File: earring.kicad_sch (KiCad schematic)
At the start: 98 parts, among them J2 USB_C_Receptacle_USB2.0, Q1 NMOS 20V 0.75A 500mΩ@4.5V, Q2 NMOS 20V 0.75A 500mΩ@4.5V, Q3 NMOS 20V 0.75A 500mΩ@4.5V, Q4 NMOS 20V 0.75A 500mΩ@4.5V, U1 Magnetic Switch, U10 USBLC6-2P6, U20 LGS4056H, U3 RP2040, U4 W25Q16JV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

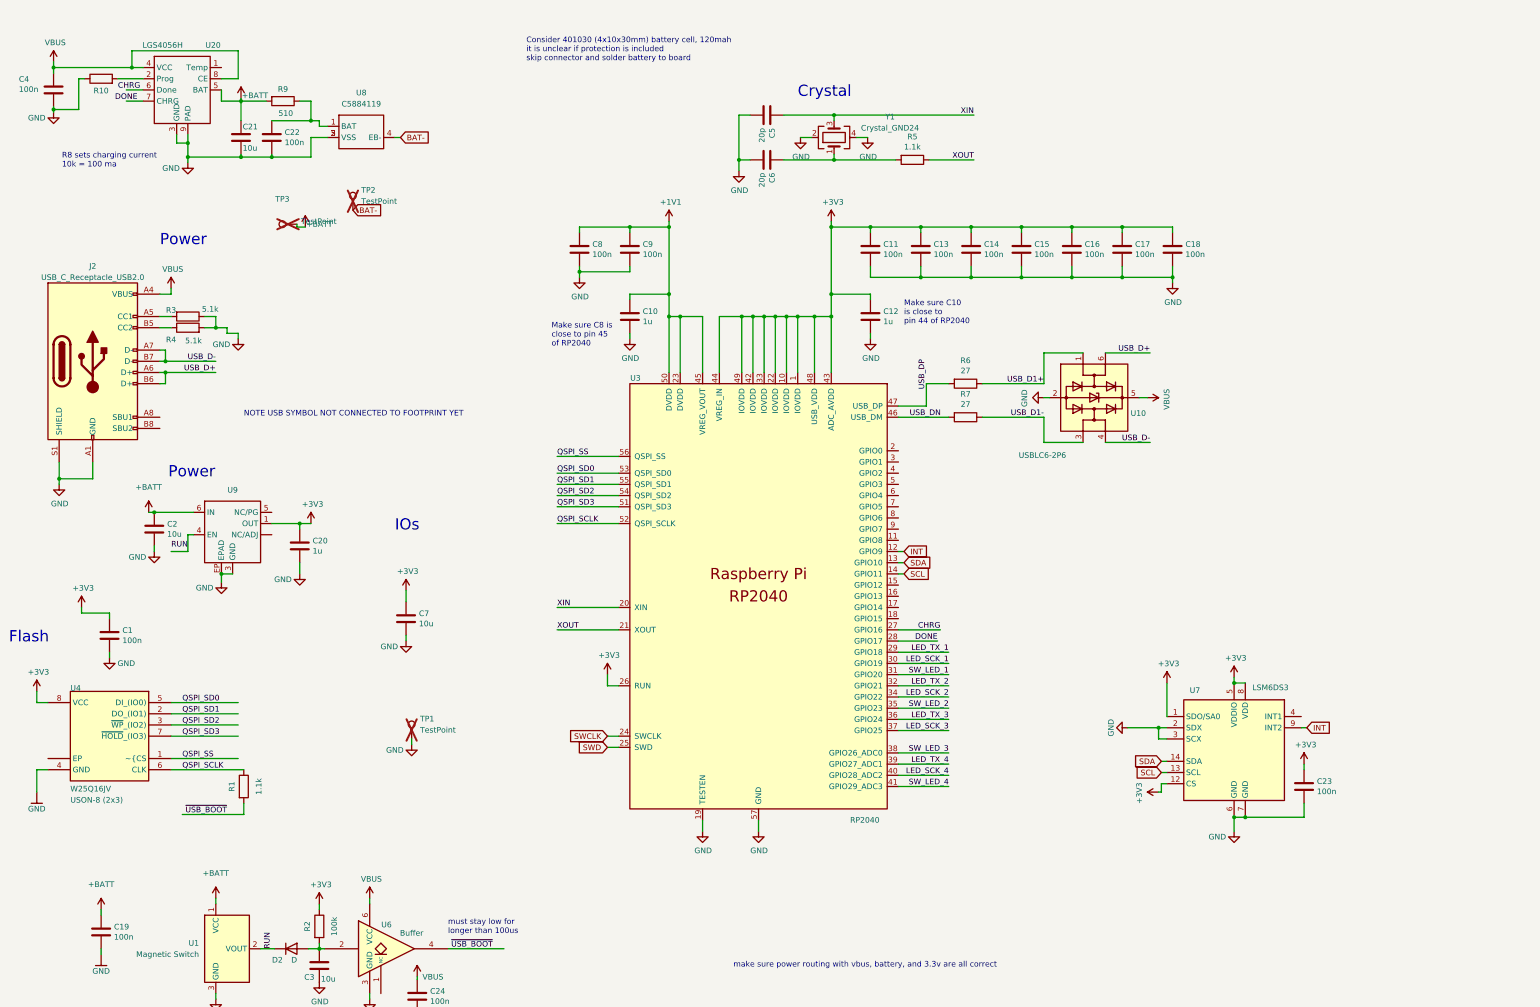
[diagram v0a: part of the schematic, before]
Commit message: Updated files, nearly complete. Added stiffener layer.
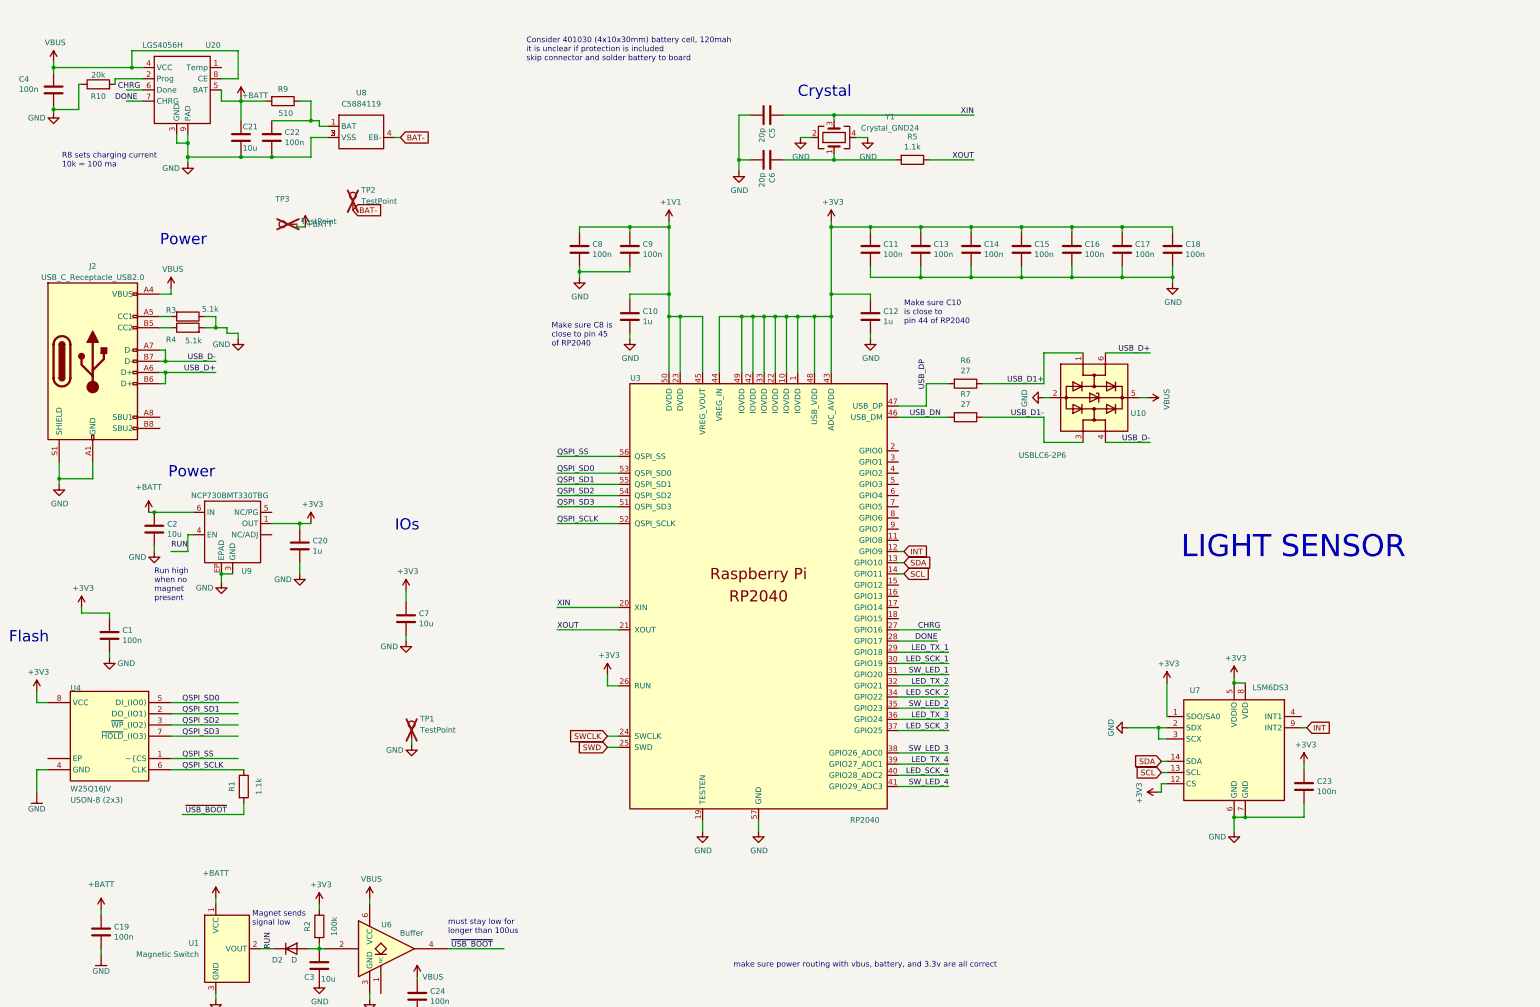
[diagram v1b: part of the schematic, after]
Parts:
- C1, C11, C13, C14, C15, C16, C17, C18, C19, C22, C23, C24, C4, C8, C9: LCSC C30926 -> C60474
- C10, C12, C20, C25, C26, C27, C28, C29, C30, C31, C32: LCSC C15849 -> C29266
- C2: LCSC C15850 -> C315248
- C5, C6: LCSC C1648 -> C107000
- R10: value ~ -> 20k; LCSC (none) -> C25765
- U6: LCSC C7598681 -> C2864615
- U9: value ~ -> NCP730BMT330TBG; LCSC (none) -> C892821
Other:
- note added: "LIGHT SENSOR"
- note added: "Magnet sends signal low"
- note added: "Run high when no magnet present"
- note removed: "NOTE USB SYMBOL NOT CONNECTED TO FOOTPRINT YET"
- moved on the sheet: R10

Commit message: Add light sensor, add more 3d models.
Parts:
- added Q5: ~, LED_SMD:LED_0603_1608Metric, symbol Sensor_Optical:KPS-3227
- added R8: WHAT VALUE?, Resistor_SMD:R_0402_1005Metric, symbol Device:R
- R3, R4: LCSC C137955 -> C25905
- U24: value ~ -> SK9822-EC20
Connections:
- net +3V3: now also Q5.1, Q5.3
- net GND: now also R8.2
- net SW_LED_3: now also U3.2 (GPIO0); no longer U3.38 (GPIO26_ADC0)
- new net LIGHT_SENSE: Q5.2, Q5.4, R8.1, U3.38 (GPIO26_ADC0)
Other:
- note removed: "LIGHT SENSOR"
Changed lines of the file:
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@@
   (junction (at 543.56 27.94) (diameter 0) (color 0 0 0 0)
   )
+  (junction (at 316.865 144.78) (diameter 0) (color 0 0 0 0)
+  )
   (junction (at 280.67 188.595) (diameter 0) (color 0 0 0 0)
   )
@@
     (stroke (width 0) (type default))
   )
+  (wire (pts (xy 316.865 156.21) (xy 316.865 153.035))
+    (stroke (width 0) (type default))
+  )
   (wire (pts (xy 202.565 107.95) (xy 202.565 95.25))
     (stroke (width 0) (type default))
@@
     (stroke (width 0) (type default))
   )
+  (wire (pts (xy 313.69 144.78) (xy 316.865 144.78))
+    (stroke (width 0) (type default))
+  )
   (wire (pts (xy 281.305 203.2) (xy 280.67 203.2))
     (stroke (width 0) (type default))
@@
     (stroke (width 0) (type default))
   )
+  (wire (pts (xy 316.865 132.08) (xy 316.865 133.985))
+    (stroke (width 0) (type default))
+  )
   (wire (pts (xy 464.82 83.82) (xy 482.6 83.82))
     (stroke (width 0) (type default))
@@
     (stroke (width 0) (type default))
   )
+  (wire (pts (xy 316.865 144.78) (xy 316.865 144.145))
+    (stroke (width 0) (type default))
+  )
   (wire (pts (xy 378.46 185.42) (xy 383.54 185.42))
     (stroke (width 0) (type default))
@@
     (stroke (width 0) (type default))
   )
+  (wire (pts (xy 316.865 145.415) (xy 316.865 144.78))
+    (stroke (width 0) (type default))
+  )
   (wire (pts (xy 574.04 195.58) (xy 579.12 195.58))
     (stroke (width 0) (type default))
@@
     (stroke (width 0) (type default))
   )
-  (wire (pts (xy 221.615 194.31) (xy 233.045 194.31))
+  (wire (pts (xy 221.615 125.73) (xy 233.045 125.73))
     (stroke (width 0) (type default))
   )
@@
     (stroke (width 0) (type default))
   )
+  (wire (pts (xy 221.615 194.31) (xy 234.95 194.31))
+    (stroke (width 0) (type default))
+  )
   (wire (pts (xy 36.195 161.29) (xy 36.195 162.56))
     (stroke (width 0) (type default))
@@
     (effects (font (size 1.27 1.27)) (justify left bottom))
   )
-  (text "LIGHT SENSOR" (at 285.75 150.495 0)
-    (effects (font (size 5 5)) (justify left bottom))
-  )
   (text "need to double check RC\nrise time considering\nbuffer flips at less than 0.7v"
     (at 72.39 259.715 0)
@@
     (effects (font (size 1.27 1.27)) (justify left bottom))
   )
-  (label "SW_LED_3" (at 233.045 194.31 180) (fields_autoplaced)
+  (label "SW_LED_3" (at 233.045 125.73 180) (fields_autoplaced)
     (effects (font (size 1.27 1.27)) (justify right bottom))
   )
@@
     (effects (font (size 1.27 1.27)) (justify right bottom))
   )
+  (label "LIGHT_SENSE" (at 313.69 144.78 180) (fields_autoplaced)
+    (effects (font (size 1.27 1.27)) (justify right bottom))
+  )
   (label "LED_SCK_1" (at 520.7 226.06 180) (fields_autoplaced)
     (effects (font (size 1.27 1.27)) (justify right bottom))
@@
     (effects (font (size 1.27 1.27)) (justify right bottom))
   )
+  (label "LIGHT_SENSE" (at 234.95 194.31 180) (fields_autoplaced)
+    (effects (font (size 1.27 1.27)) (justify right bottom))
+  )
   (label "DONE" (at 230.505 168.91 180) (fields_autoplaced)
     (effects (font (size 1.27 1.27)) (justify right bottom))
@@
     )
   )
+  (symbol (lib_id "power:+3V3") (at 316.865 132.08 0) (unit 1)
+    (in_bom yes) (on_board yes) (dnp no)
+    (property "Reference" "#PWR050" (at 316.865 135.89 0)
+      (effects (font (size 1.27 1.27)) hide)
+    )
+    (property "Value" "+3V3" (at 317.246 127.6858 0)
+      (effects (font (size 1.27 1.27)))
+    )
+    (property "Footprint" "" (at 316.865 132.08 0)
+      (effects (font (size 1.27 1.27)) hide)
+    )
+    (property "Datasheet" "" (at 316.865 132.08 0)
+      (effects (font (size 1.27 1.27)) hide)
+    )
+    (pin "1")
+    (instances
+      (project "earring"
+        (path "/10ff4ace-8dac-45ce-94a5-ae8ae7d42914"
+          (reference "#PWR050") (unit 1)
+        )
+      )
+    )
+  )
   (symbol (lib_id "earring:SK9822") (at 561.34 73.66 0) (unit 1)
     (in_bom yes) (on_board yes) (dnp no) (fields_autoplaced)
@@
     )
   )
+  (symbol (lib_id "Device:R") (at 316.865 149.225 0) (unit 1)
+    (in_bom yes) (on_board yes) (dnp no)
+    (property "Reference" "R8" (at 313.5122 150.495 90)
+      (effects (font (size 1.27 1.27)))
+    )
+    (property "Value" "WHAT VALUE?" (at 324.0786 146.05 0)
+      (effects (font (size 1.27 1.27)))
+    )
+    (property "Footprint" "Resistor_SMD:R_0402_1005Metric" (at 315.087 149.225 90)
+      (effects (font (size 1.27 1.27)) hide)
+    )
+    (property "Datasheet" "~" (at 316.865 149.225 0)
+      (effects (font (size 1.27 1.27)) hide)
+    )
+    (property "LCSC" "" (at 316.865 149.225 90)
+      (effects (font (size 1.27 1.27)) hide)
+    )
+    (pin "1")
+    (pin "2")
+    (instances
+      (project "earring"
+        (path "/10ff4ace-8dac-45ce-94a5-ae8ae7d42914"
+          (reference "R8") (unit 1)
+        )
+      )
+    )
+  )
   (symbol (lib_id "earring:SK9822") (at 480.06 162.56 0) (unit 1)
     (in_bom yes) (on_board yes) (dnp no) (fields_autoplaced)
@@
       (effects (font (size 1.27 1.27)) (justify left))
     )
-    (property "Value" "~" (at 440.69 35.56 0)
-      (effects (font (size 1.27 1.27)))
+    (property "Value" "SK9822-EC20" (at 440.69 35.56 0)
+      (effects (font (size 1.27 1.27)) hide)
     )
     (property "Footprint" "parts:LED-SK9822-EC20" (at 440.69 35.56 0)
@@
       (effects (font (size 1.27 1.27)) hide)
     )
-    (property "LCSC" "C137955" (at 60.325 97.79 90)
+    (property "LCSC" "C25905" (at 60.325 97.79 90)
       (effects (font (size 1.27 1.27)) hide)
     )
@@
       (effects (font (size 1.27 1.27)) hide)
     )
-    (property "LCSC" "C137955" (at 60.325 95.25 90)
+    (property "LCSC" "C25905" (at 60.325 95.25 90)
       (effects (font (size 1.27 1.27)) hide)
     )
@@
     )
   )
+  (symbol (lib_id "power:GND") (at 316.865 156.21 0) (unit 1)
+    (in_bom yes) (on_board yes) (dnp no)
+    (property "Reference" "#PWR053" (at 316.865 162.56 0)
+      (effects (font (size 1.27 1.27)) hide)
+    )
+    (property "Value" "GND" (at 313.055 157.48 0)
+      (effects (font (size 1.27 1.27)))
+    )
+    (property "Footprint" "" (at 316.865 156.21 0)
+      (effects (font (size 1.27 1.27)) hide)
+    )
+    (property "Datasheet" "" (at 316.865 156.21 0)
+      (effects (font (size 1.27 1.27)) hide)
+    )
+    (pin "1")
+    (instances
+      (project "earring"
+        (path "/10ff4ace-8dac-45ce-94a5-ae8ae7d42914"
+          (reference "#PWR053") (unit 1)
+        )
+      )
+    )
+  )
   (symbol (lib_id "power:+BATT") (at 525.78 93.98 0) (unit 1)
     (in_bom yes) (on_board yes) (dnp no)
@@
         )
       )
+    )
+  )
+  (symbol (lib_id "Sensor_Optical:KPS-3227") (at 316.865 139.065 0) (unit 1)
+    (in_bom yes) (on_board yes) (dnp no) (fields_autoplaced)
+    (property "Reference" "Q5" (at 320.04 137.0457 0)
+      (effects (font (size 1.27 1.27)) (justify left))
+    )
+    (property "Value" "~" (at 320.04 139.5857 0)
+      (effects (font (size 1.27 1.27)) (justify left))
+    )
+    (property "Footprint" "LED_SMD:LED_0603_1608Metric" (at 316.865 135.255 0)
+      (effects (font (size 1.27 1.27)) hide)
+    )
+    (property "Datasheet" "" (at 316.865 135.255 0)
+      (effects (font (size 1.27 1.27)) hide)
+    )
+    (pin "3")
+    (pin "4")
+    (pin "2")
+    (pin "1")
+    (instances
+      (project "earring"
+        (path "/10ff4ace-8dac-45ce-94a5-ae8ae7d42914"
+          (reference "Q5") (unit 1)
+        )
+      )

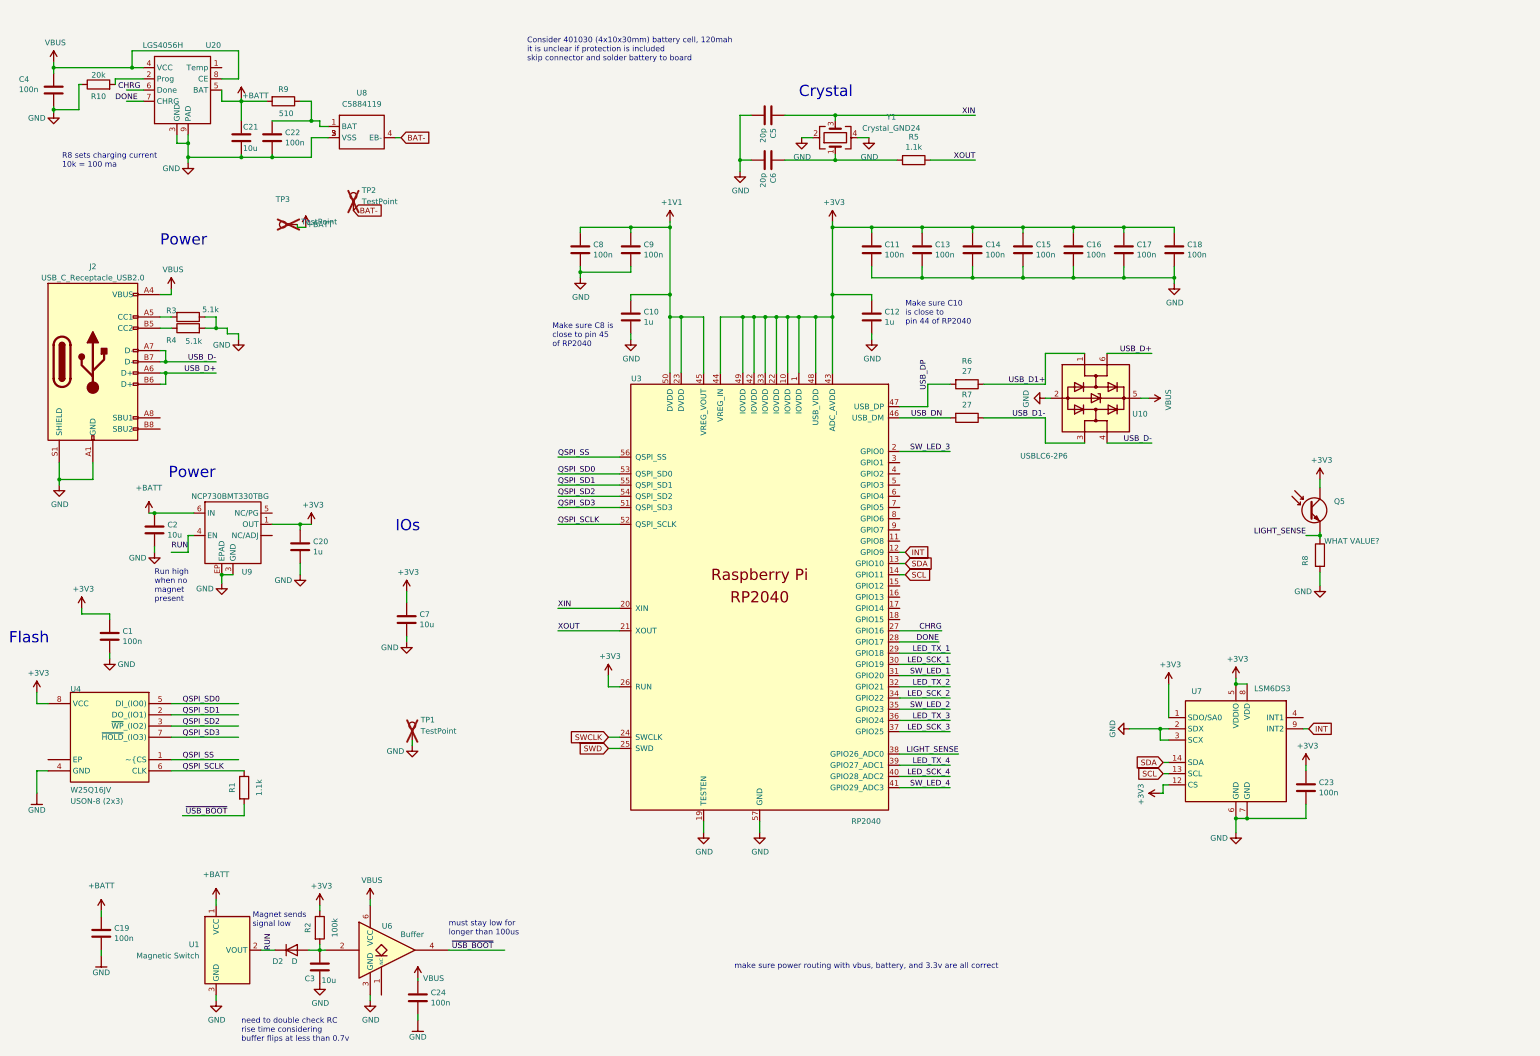
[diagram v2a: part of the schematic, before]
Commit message: added silkscreen, debug contacts, and voltage monitoring
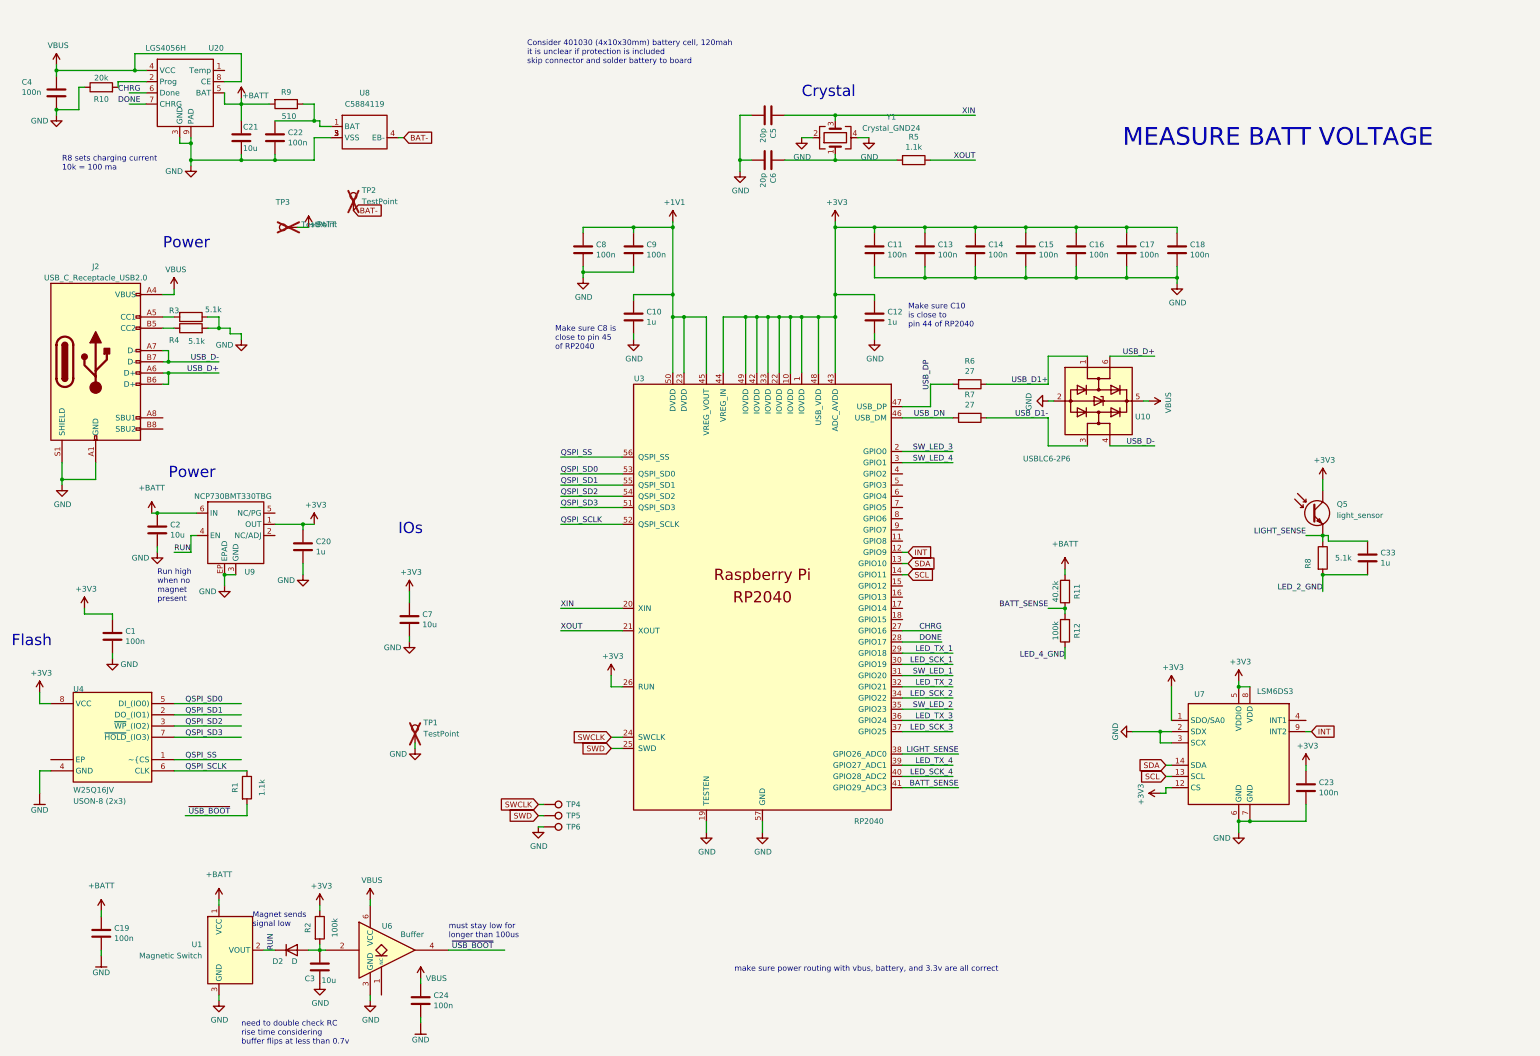
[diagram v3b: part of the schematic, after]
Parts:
- removed Q5: ~, LED_SMD:LED_0603_1608Metric, symbol Sensor_Optical:KPS-3227
- added C33: 1u, Capacitor_SMD:C_0402_1005Metric, symbol Device:C
- added Q5: light_sensor, LED_SMD:LED_0603_1608Metric, symbol earring:light_sensor
- added R11: 40.2k, Resistor_SMD:R_0402_1005Metric, symbol Device:R
- added R12: 100k, Resistor_SMD:R_0402_1005Metric, symbol Device:R
- added TP4, TP5, TP6: TestPoint, TestPoint:TestPoint_Pad_1.0x1.0mm, symbol Connector:TestPoint
- R8: value WHAT VALUE? -> 5.1k; LCSC (none) -> C25905
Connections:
- net +3V3: now also Q5.1
- net +BATT: now also R11.2
- net GND: now also TP6.1; no longer R8.2
- net LED_2_GND: now also R8.2, C33.2
- net LED_4_GND: now also R12.1
- net LIGHT_SENSE: now also C33.1, Q5.2
- net SWCLK: now also TP4.1
- net SWD: now also TP5.1
- net SW_LED_4: now also U3.3 (GPIO1); no longer U3.41 (GPIO29_ADC3)
- new net BATT_SENSE: R11.1, R12.2, U3.41 (GPIO29_ADC3)
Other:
- note added: "MEASURE BATT VOLTAGE"
- moved on the sheet: C1, C10, C11, C12, C13, C14, C15, C16, C17, C18, C2, C20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
